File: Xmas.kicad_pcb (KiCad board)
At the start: 2 copper layers, 50 x 60.6 mm, 55 parts, among them IC1 STM32C011F6, IC2 TP4056-42, Q1 AO3401A, Q2 CJ3400, SW1 BZCN_TSA007A1518B03, SW2 BZCN_TSA007A1518B03

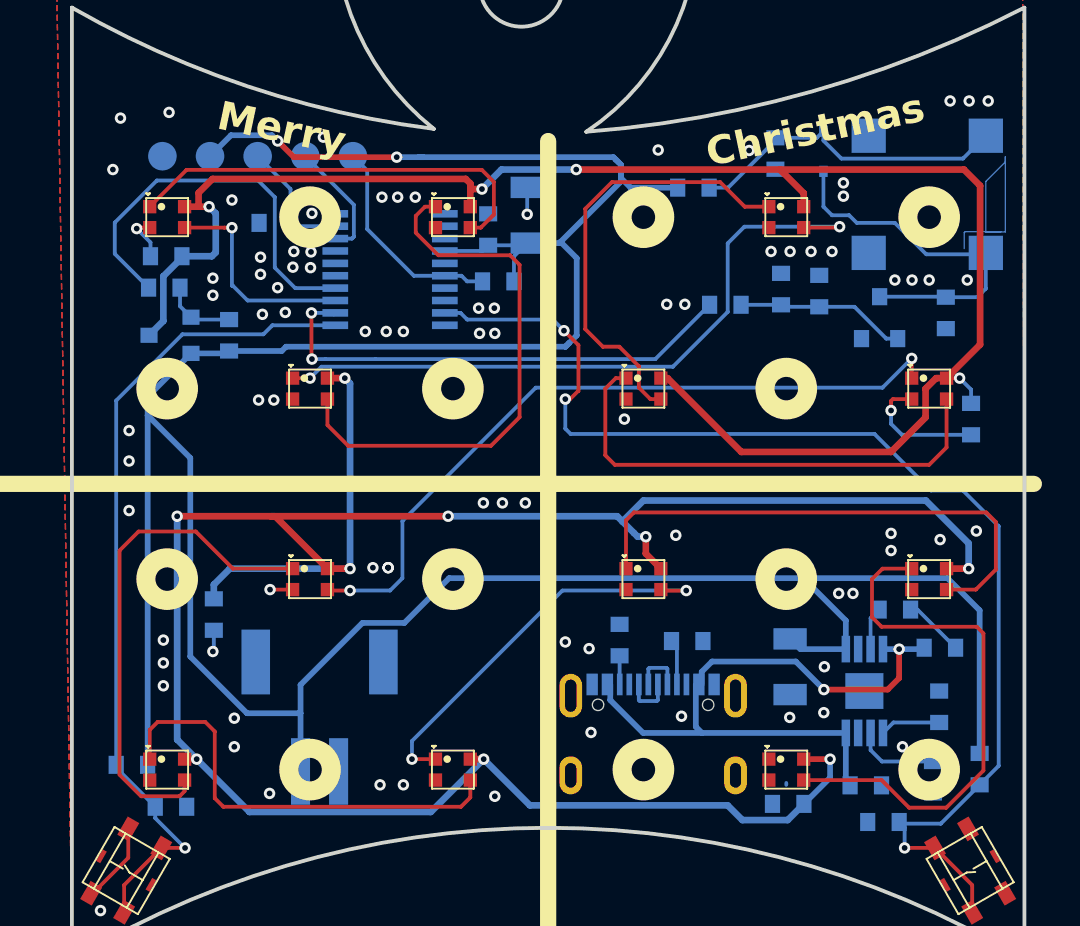
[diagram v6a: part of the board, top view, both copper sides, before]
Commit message: Update footprints and PCB have 3D models of components
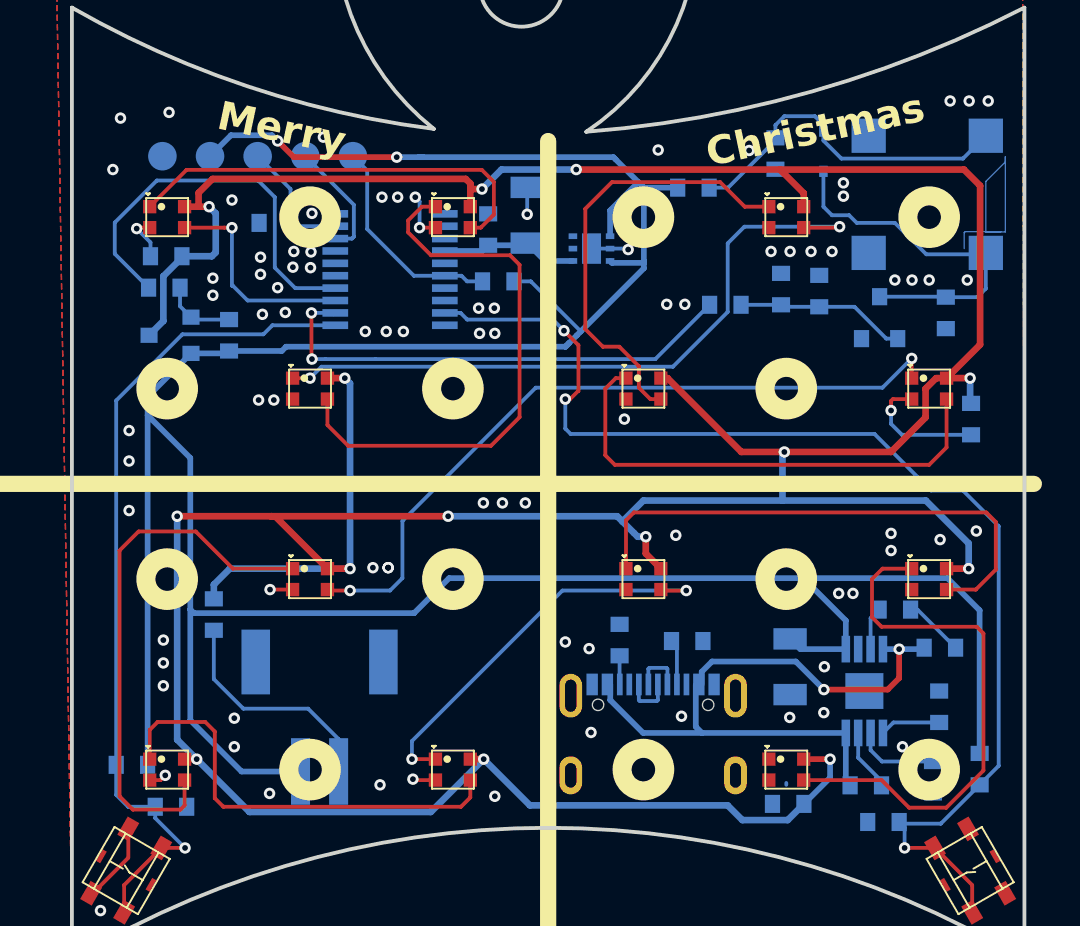
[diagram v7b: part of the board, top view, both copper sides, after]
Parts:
- added U1: TPS7A2633DRVR, BornaKiCadLibrary:WSON-6, B.Cu at (127.3, 82.7)
- C1, C10, C11, C12, C13, C2, C4, C5, C6, C7, C9: footprint Borna KiCAD Library:C0603 -> BornaKiCadLibrary:C0603
- C3, C8: footprint Borna KiCAD Library:C1206 -> BornaKiCadLibrary:C1206
- CONN1: footprint Borna KiCAD Library:JST_S2B-PH-SM4-TB -> BornaKiCadLibrary:JST_S2B-PH-SM4-TB
- CONN2: footprint Borna KiCAD Library:TYPE-C_16PIN_2MD(073) -> BornaKiCadLibrary:TYPE-C_16PIN_2MD(073)
- D1: footprint Borna KiCAD Library:SOD323 -> BornaKiCadLibrary:SOD323
- IC1: footprint Borna KiCAD Library:TSSOP20 -> BornaKiCadLibrary:TSSOP20
- IC2: footprint Borna KiCAD Library:EMSOP -> BornaKiCadLibrary:EMSOP
- LED1, LED10, LED11, LED12, LED2, LED3, LED4, LED5, LED6, LED7, LED8, LED9: footprint Borna KiCAD Library:WS2812B-2020 -> BornaKiCadLibrary:WS2812B-2020
- LED13: footprint Borna KiCAD Library:LED_0603 -> BornaKiCadLibrary:LED_0603
- Q1, Q2: footprint Borna KiCAD Library:SOT-23-3L -> BornaKiCadLibrary:SOT-23-3L
- R1, R10, R11, R12, R13, R14, R2, R3, R4, R5, R6, R7, R8, R9: footprint Borna KiCAD Library:R0603 -> BornaKiCadLibrary:R0603
- SPK1: footprint Borna KiCAD Library:MTL-7525 -> BornaKiCadLibrary:MTL-7525
- SW1, SW2: footprint Borna KiCAD Library:TSA007A1518B03 -> BornaKiCadLibrary:TSA007A1518B03
- TP1, TP2, TP3, TP4, TP5: footprint Borna KiCAD Library:TP-1_5mm -> BornaKiCadLibrary:TP-1_5mm
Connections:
- C7 pad 2: VDD -> 3V3
- C8 pad 2: VDD -> 3V3
- IC1 pad 4: VDD -> 3V3
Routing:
- net GND: track 17.2 -> 38.0 mm, vias 86 -> 88
- net 3V3: track 0.00 -> 7.28 mm
- net VDD: track 167.8 -> 170.8 mm
- net WS_SUPPLY: track 217.7 -> 220.7 mm, vias 13 -> 14
- net Net-(LED7-DO): track 26.7 -> 28.3 mm
- net Net-(C13-Pad2): track 17.4 -> 18.7 mm
- net /BTN2: track 43.4 -> 44.4 mm
- net Net-(LED2-DO): track 28.8 -> 29.4 mm

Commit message: PCB is finished
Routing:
- net GND: track 38.0 -> 38.9 mm, vias 88 -> 93
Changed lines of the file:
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@@
 		)
 	)
+	(gr_arc
+		(start 129.199998 65.233913)
+		(mid 128.992423 71.826829)
+		(end 124.9 77)
+		(stroke
+			(width 0.85)
+			(type default)
+		)
+		(layer "F.SilkS")
+	)
 	(gr_circle
 		(center 145 81)
@@
 		(layer "F.SilkS")
 	)
+	(gr_arc
+		(start 118.400982 65.66213)
+		(mid 120.943651 64.441505)
+		(end 123.555786 65.505386)
+		(stroke
+			(width 0.85)
+			(type default)
+		)
+		(layer "F.SilkS")
+	)
 	(gr_circle
 		(center 112.5 110)
@@
 		(layer "F.SilkS")
 	)
+	(gr_arc
+		(start 123.857893 65.306745)
+		(mid 126.494213 64.044615)
+		(end 129.199999 65.150001)
+		(stroke
+			(width 0.85)
+			(type default)
+		)
+		(layer "F.SilkS")
+	)
 	(gr_circle
 		(center 120 100)
@@
 		(layer "F.SilkS")
 	)
+	(gr_arc
+		(start 124.90927 77.052473)
+		(mid 119.468473 72.705383)
+		(end 118.400982 65.823529)
+		(stroke
+			(width 0.85)
+			(type default)
+		)
+		(layer "F.SilkS")
+	)
 	(gr_circle
 		(center 130 81)
@@
 	)
 	(segment
-		(start 147.9 82.95)
-		(end 147.975 82.875)
-		(width 0.2)
-		(layer "B.Cu")
-		(net 13)
-	)
-	(segment
 		(start 147.525 85.2)
 		(end 147.975 84.75)
@@
 	)
 	(segment
-		(start 143.2 81.3)
-		(end 144.85 82.95)
+		(start 147.975 84.75)
+		(end 147.975 82.875)
 		(width 0.2)
 		(layer "B.Cu")
@@
 	)
 	(segment
-		(start 141.2 81.3)
-		(end 143.2 81.3)
+		(start 143.2 81.3)
+		(end 144.85 82.95)
 		(width 0.2)
 		(layer "B.Cu")
@@
 	)
 	(segment
-		(start 144.85 82.95)
-		(end 147.9 82.95)
+		(start 141.2 81.3)
+		(end 143.2 81.3)
 		(width 0.2)
 		(layer "B.Cu")
@@
 	)
 	(segment
-		(start 147.975 84.75)
-		(end 147.975 82.875)
+		(start 144.85 82.95)
+		(end 147.9 82.95)
 		(width 0.2)
 		(layer "B.Cu")
@@
 	)
 	(segment
+		(start 129.085 91.435)
+		(end 129.1 91.45)
+		(width 0.2)
+		(layer "F.Cu")
+		(net 23)
+	)
+	(segment
 		(start 104.65 110.55)
 		(end 104.9 110.3)
@@
 	)
 	(segment
+		(start 129.085 90.55)
+		(end 129.085 91.435)
+		(width 0.2)
+		(layer "F.Cu")
+		(net 23)
+	)
+	(segment
 		(start 102.958975 113.111251)
 		(end 102.958975 114.629774)
@@
 	)
 	(via
+		(at 131.5 88.05)
+		(size 0.6)
+		(drill 0.3)
+		(layers "F.Cu" "B.Cu")
+		(free yes)
+		(net 23)
+	)
+	(via
 		(at 104.8 104.4)
 		(size 0.6)
@@
 	)
 	(via
+		(at 140.3 87.5)
+		(size 0.6)
+		(drill 0.3)
+		(layers "F.Cu" "B.Cu")
+		(free yes)
+		(net 23)
+	)
+	(via
 		(at 121.6 96)
 		(size 0.6)
@@
 	)
 	(via
-		(at 125.9 103.3)
+		(at 126.1 103.65)
 		(size 0.6)
 		(drill 0.3)
@@
 	)
 	(via
+		(at 140.05 94.9)
+		(size 0.6)
+		(drill 0.3)
+		(layers "F.Cu" "B.Cu")
+		(free yes)
+		(net 23)
+	)
+	(via
+		(at 128.8 101.3)
+		(size 0.6)
+		(drill 0.3)
+		(layers "F.Cu" "B.Cu")
+		(free yes)
+		(net 23)
+	)
+	(via
 		(at 132 107.2)
 		(size 0.6)
@@
 	)
 	(via
-		(at 129 91.6)
+		(at 129.1 91.45)
 		(size 0.6)
 		(drill 0.3)
@@
 		(net 23)
 	)
+	(via
+		(at 138.3 76.9)
+		(size 0.6)
+		(drill 0.3)
+		(layers "F.Cu" "B.Cu")
+		(free yes)
+		(net 23)
+	)
 	(segment
 		(start 143 91.85)
@@
 	)
 	(segment
-		(start 133.475 85.6)
-		(end 130.625 88.45)
+		(start 132.725 86.35)
+		(end 131.65 86.35)
 		(width 0.2)
 		(layer "B.Cu")
@@
 	)
 	(segment
-		(start 113.3 88.45)
+		(start 129.55 88.45)
 		(end 112.6 88.45)
 		(width 0.2)
@@
 	)
 	(segment
-		(start 115.95 88.45)
-		(end 113.3 88.45)
+		(start 113.74 86.11)
+		(end 113.825 86.025)
 		(width 0.2)
 		(layer "B.Cu")
@@
 	)
 	(segment
-		(start 113.74 86.11)
-		(end 113.825 86.025)
+		(start 133.475 85.6)
+		(end 132.725 86.35)
 		(width 0.2)
 		(layer "B.Cu")
@@
 	)
 	(segment
-		(start 130.625 88.45)
-		(end 115.95 88.45)
+		(start 131.65 86.35)
+		(end 129.55 88.45)
 		(width 0.2)
 		(layer "B.Cu")
